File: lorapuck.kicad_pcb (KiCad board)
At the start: 4 copper layers, 30 x 43 mm, 53 parts, among them J1 USB_C_Receptacle_USB2.0_16P, SW1 BOOTSEL, SW2 RESET, U1 SX1262IMLTRT, U2 RP2040, U3 W25Q128JVS, U4 PE4259, U5 AP2112K-3.3, U6 SHTC3, Y1 32MHz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

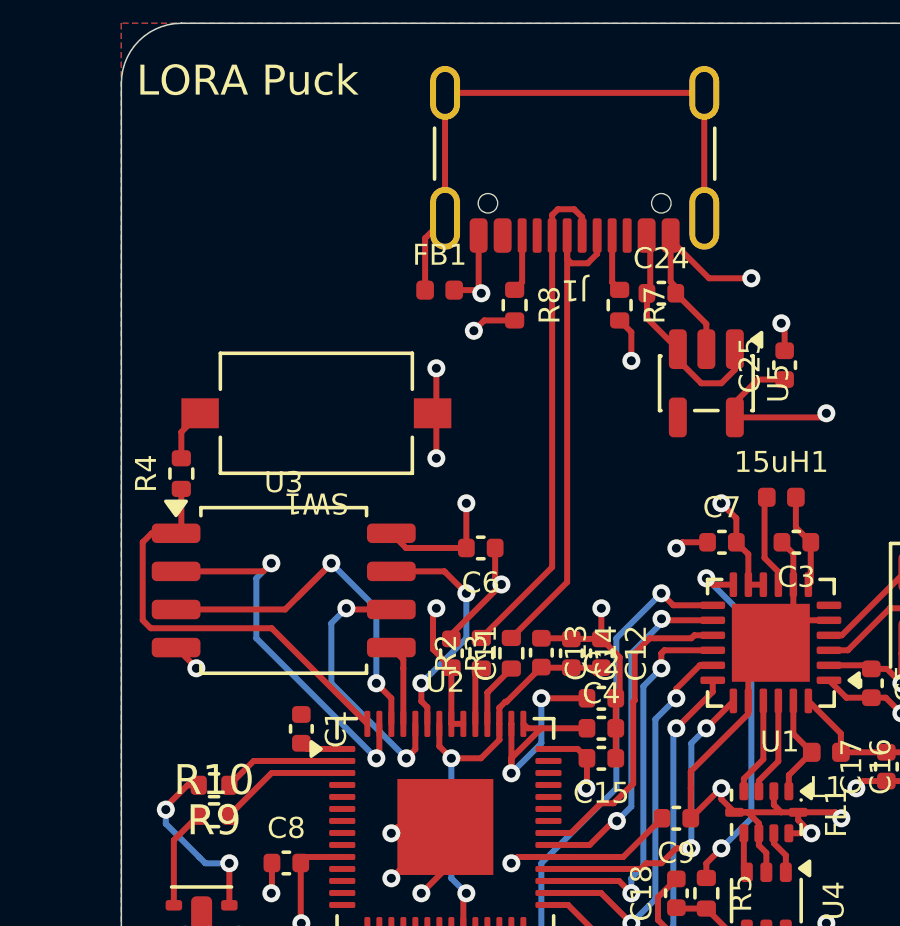
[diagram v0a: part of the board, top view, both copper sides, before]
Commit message: fixed some issues with pcb
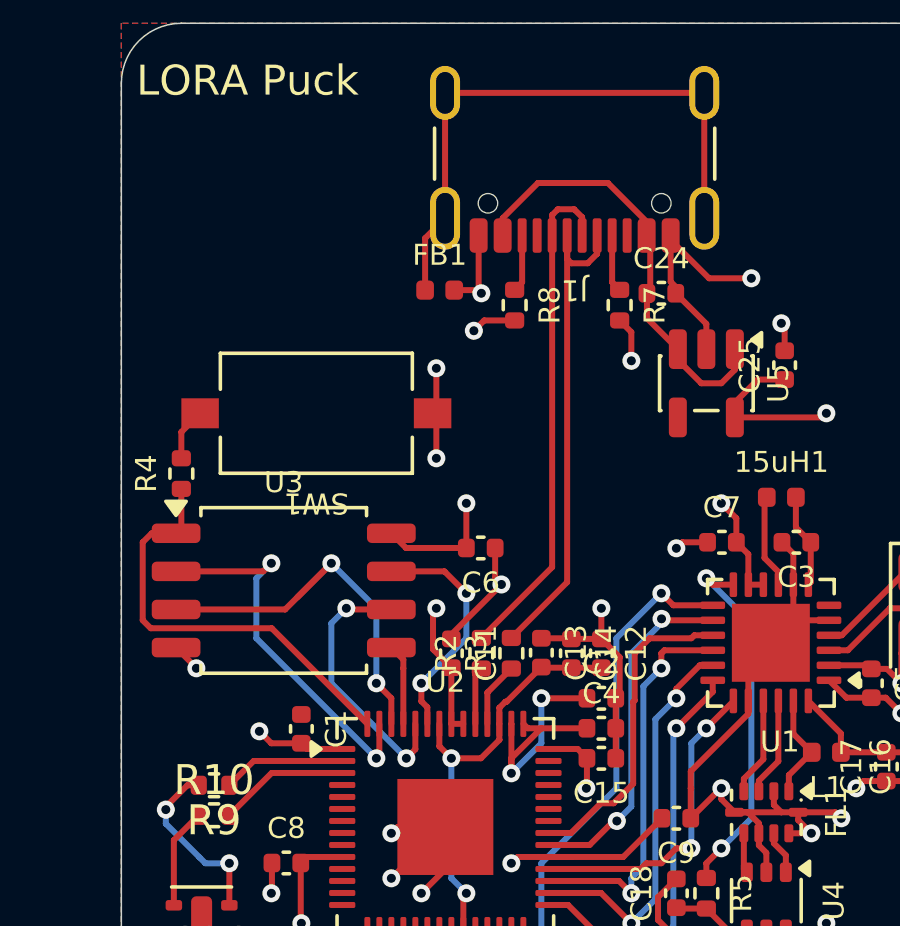
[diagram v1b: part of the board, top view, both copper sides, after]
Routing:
- net VBUS: track 7.94 -> 14.8 mm
- net +3V3: track 53.6 -> 55.2 mm, vias 14 -> 15
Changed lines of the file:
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@@
+	)
+	(segment
+		(start 83 104)
+		(end 82.6 103.6)
+		(width 0.2)
+		(layer "F.Cu")
+		(net 4)
+	)
+	(segment
+		(start 85.3625 107.79)
+		(end 84.18 107.79)
+		(width 0.2)
+		(layer "F.Cu")
+		(net 4)
 	)
 	(segment
@@
 	)
 	(segment
+		(start 84 104)
+		(end 83 104)
+		(width 0.2)
+		(layer "F.Cu")
+		(net 4)
+	)
+	(segment
 		(start 100.15 110.2)
 		(end 101.3 110.2)
@@
 	)
 	(segment
+		(start 98.5 96.5)
+		(end 98 96)
+		(width 0.2)
+		(layer "F.Cu")
+		(net 4)
+	)
+	(segment
+		(start 101.3625 93.1375)
+		(end 101.5 93)
+		(width 0.2)
+		(layer "F.Cu")
+		(net 4)
+	)
+	(segment
+		(start 94.73 107.79)
+		(end 96.02 106.5)
+		(width 0.2)
+		(layer "F.Cu")
+		(net 4)
+	)
+	(segment
+		(start 101.3 110.2)
+		(end 101.5 110)
+		(width 0.2)
+		(layer "F.Cu")
+		(net 4)
+	)
+	(segment
+		(start 89 112)
+		(end 89.5 111.5)
+		(width 0.2)
+		(layer "F.Cu")
+		(net 4)
+	)
+	(segment
+		(start 91 103.3525)
+		(end 91.002 103.3545)
+		(width 0.2)
+		(layer "F.Cu")
+		(net 4)
+	)
+	(segment
+		(start 93 107.79)
+		(end 94.73 107.79)
+		(width 0.2)
+		(layer "F.Cu")
+		(net 4)
+	)
+	(segment
+		(start 91.5475 103.5)
+		(end 92 103.5)
+		(width 0.2)
+		(layer "F.Cu")
+		(net 4)
+	)
+	(segment
+		(start 81.6 110.4)
+		(end 81.6 111.6)
+		(width 0.2)
+		(layer "F.Cu")
+		(net 4)
+	)
+	(segment
 		(start 84.18 107.79)
 		(end 83.98 107.99)
@@
 		(net 4)
 	)
-	(segment
-		(start 98.5 96.5)
-		(end 98 96)
-		(width 0.2)
-		(layer "F.Cu")
-		(net 4)
-	)
-	(segment
-		(start 101.3625 93.1375)
-		(end 101.5 93)
-		(width 0.2)
-		(layer "F.Cu")
-		(net 4)
-	)
-	(segment
-		(start 94.73 107.79)
-		(end 96.02 106.5)
-		(width 0.2)
-		(layer "F.Cu")
-		(net 4)
-	)
-	(segment
-		(start 101.3 110.2)
-		(end 101.5 110)
-		(width 0.2)
-		(layer "F.Cu")
-		(net 4)
-	)
-	(segment
-		(start 89 112)
-		(end 89.5 111.5)
-		(width 0.2)
-		(layer "F.Cu")
-		(net 4)
-	)
-	(segment
-		(start 91 103.3525)
-		(end 91.002 103.3545)
-		(width 0.2)
-		(layer "F.Cu")
-		(net 4)
-	)
-	(segment
-		(start 85.3625 107.79)
-		(end 84.18 107.79)
-		(width 0.2)
-		(layer "F.Cu")
-		(net 4)
-	)
-	(segment
-		(start 93 107.79)
-		(end 94.73 107.79)
-		(width 0.2)
-		(layer "F.Cu")
-		(net 4)
-	)
-	(segment
-		(start 91.5475 103.5)
-		(end 92 103.5)
-		(width 0.2)
-		(layer "F.Cu")
-		(net 4)
-	)
-	(segment
-		(start 81.6 110.4)
-		(end 81.6 111.6)
-		(width 0.2)
-		(layer "F.Cu")
-		(net 4)
-	)
 	(via
 		(at 89.5 111.5)
@@
 	(via
 		(at 104 103)
+		(size 0.6)
+		(drill 0.3)
+		(layers "F.Cu" "B.Cu")
+		(free yes)
+		(net 4)
+	)
+	(via
+		(at 82.6 103.6)
 		(size 0.6)
 		(drill 0.3)
@@
 	)
 	(segment
+		(start 90.71 86.500001)
+		(end 90.71 87.075)
+		(width 0.2)
+		(layer "F.Cu")
+		(net 12)
+	)
+	(segment
+		(start 94.217824 85.324)
+		(end 91.886001 85.324)
+		(width 0.2)
+		(layer "F.Cu")
+		(net 12)
+	)
+	(segment
 		(start 98.45 91.55)
 		(end 98.45 90.8625)
@@
 	)
 	(segment
+		(start 95.51 87.075)
+		(end 95.51 86.616176)
+		(width 0.2)
+		(layer "F.Cu")
+		(net 12)
+	)
+	(segment
 		(start 95.52 89)
 		(end 95.52 89.8325)
@@
 		(width 0.2)
 		(layer "F.Cu")
+		(net 12)
+	)
+	(segment
+		(start 95.51 86.616176)
+		(end 94.217824 85.324)
+		(width 0.2)
+		(layer "F.Cu")
+		(net 12)
+	)
+	(segment
+		(start 91.886001 85.324)
+		(end 90.71 86.500001)
+		(width 0.2)
+		(layer "F.Cu")
